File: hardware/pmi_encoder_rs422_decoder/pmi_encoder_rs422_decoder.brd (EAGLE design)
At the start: 50 x 50 mm, 31 parts, among them IC1 SN75ALS193DRE4, IC2 SN75ALS193DRE4

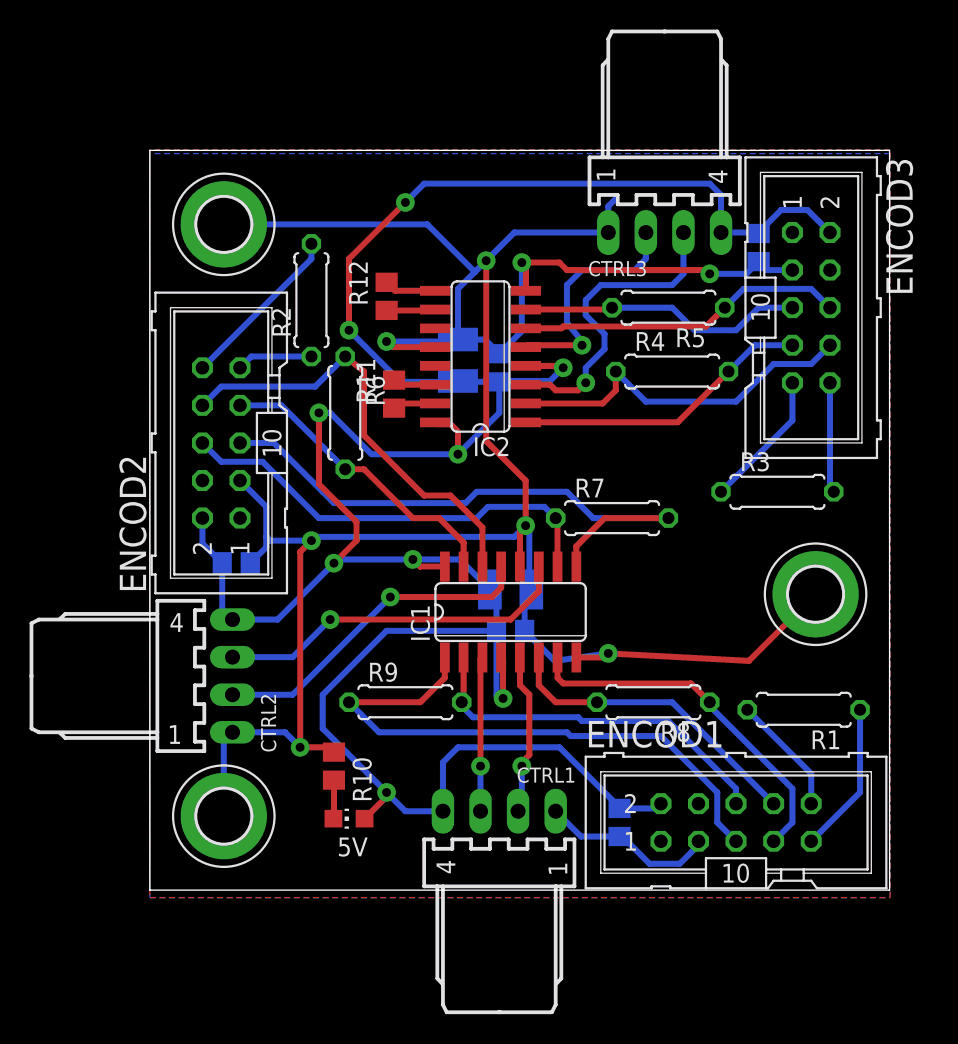
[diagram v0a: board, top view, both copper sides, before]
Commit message: some text added, silkscreen placed
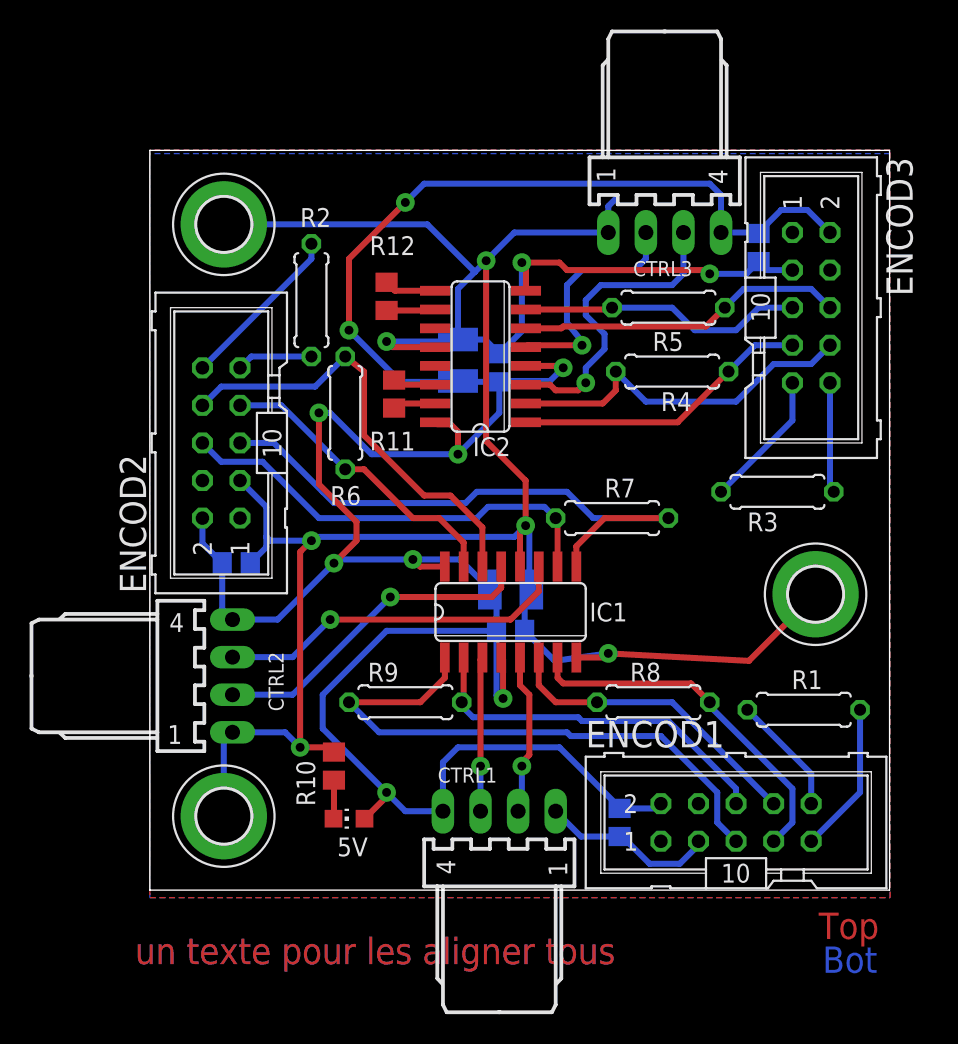
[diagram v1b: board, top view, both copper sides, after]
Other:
- board text added: "Bot"
- board text added: "Top"
- board text added: "un texte pour les aligner tous"
